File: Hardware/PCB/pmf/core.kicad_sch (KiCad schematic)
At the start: 43 parts, among them U1 AS3320, U2 TL072

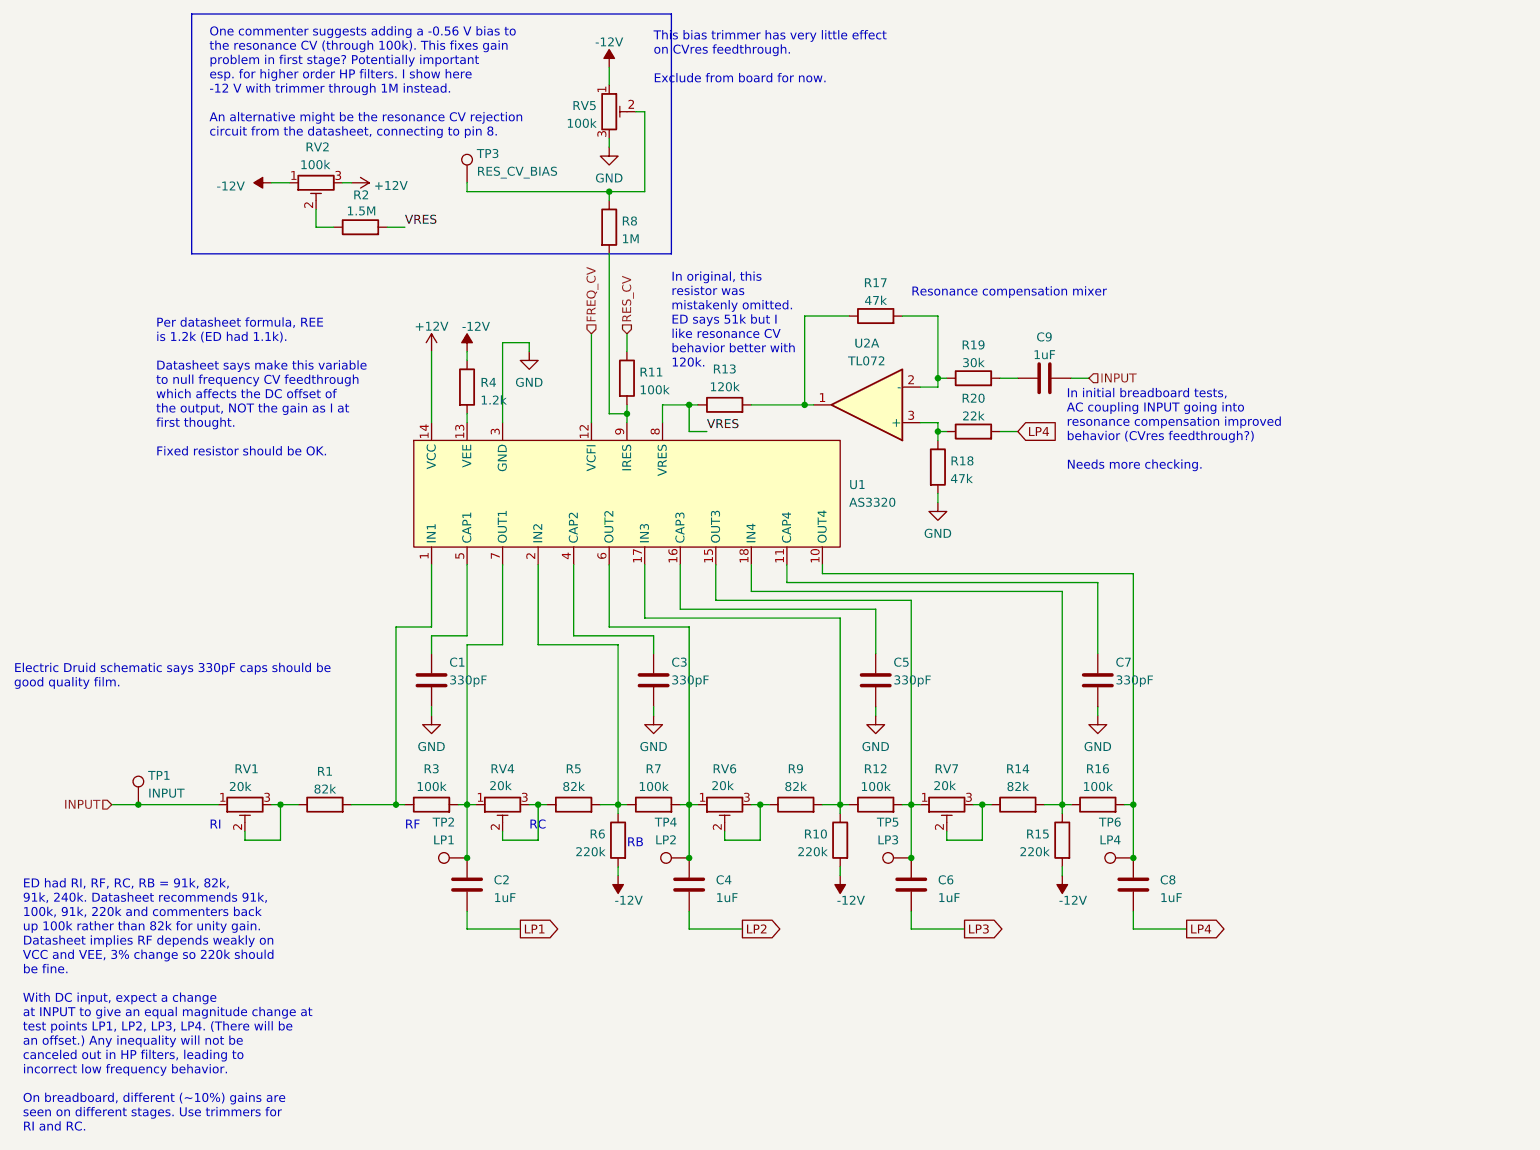
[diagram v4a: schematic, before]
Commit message: Remove VRES bias
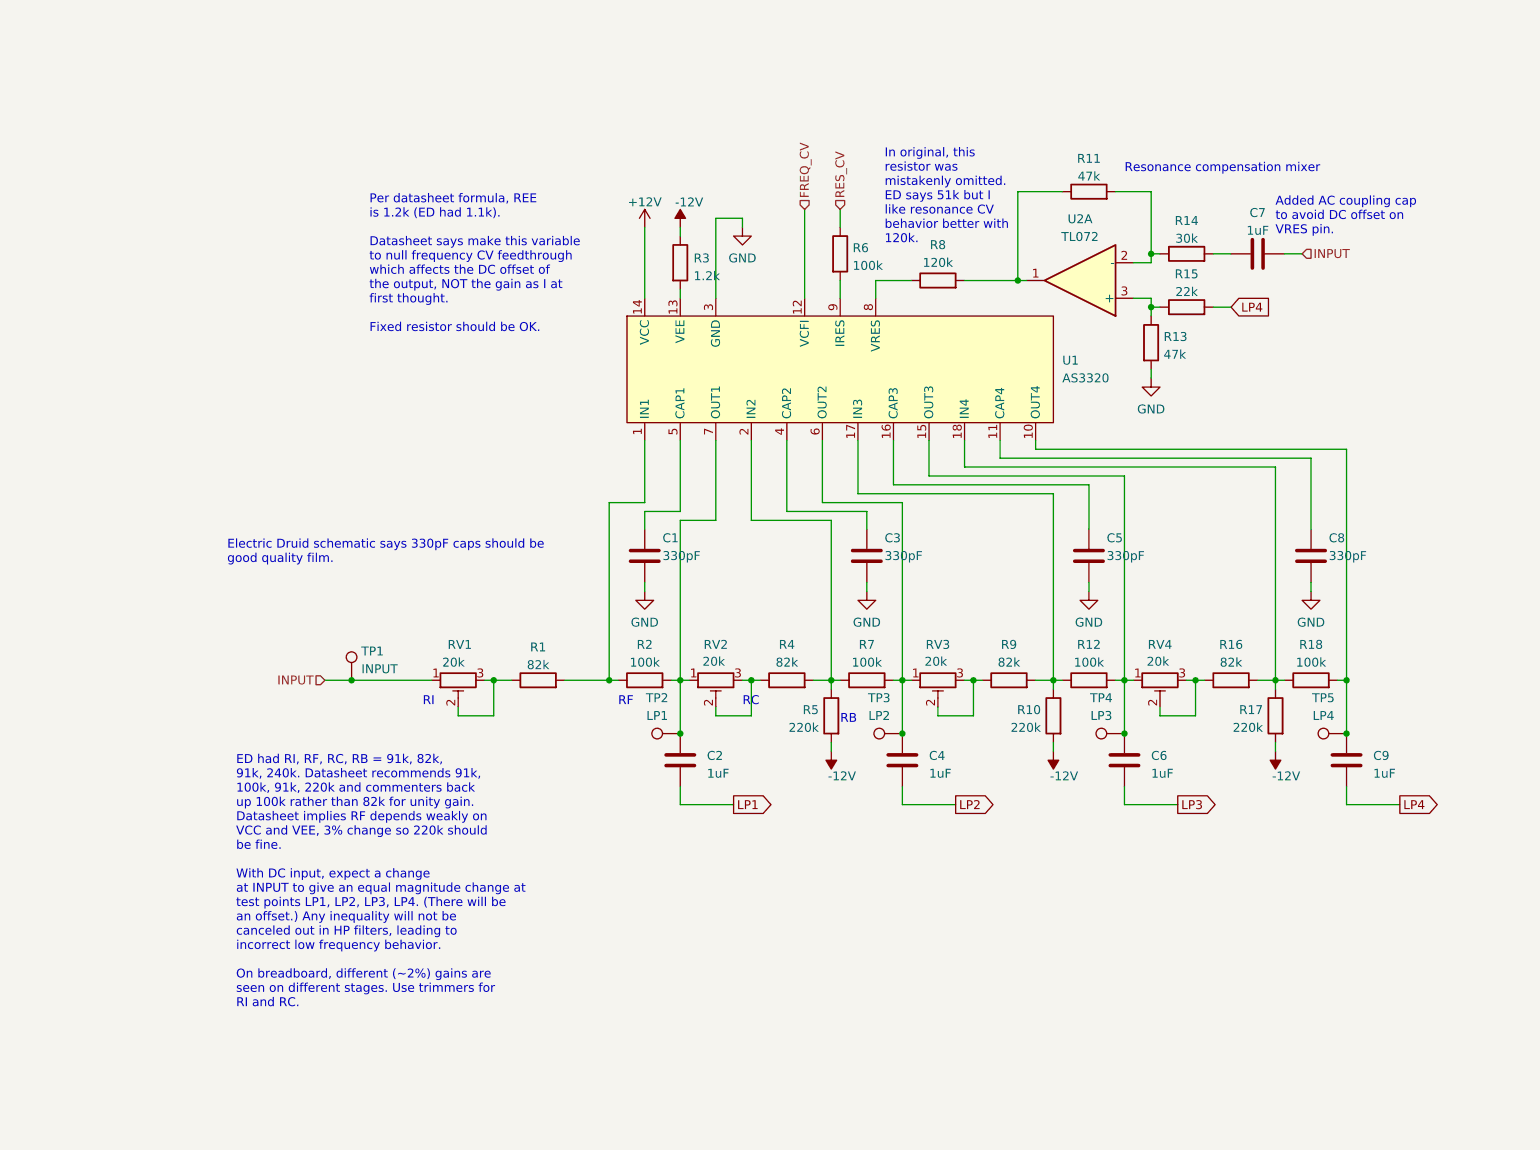
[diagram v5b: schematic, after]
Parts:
- removed R2: 1.5M, AO_tht:R_Axial_DIN0207_L6.3mm_D2.5mm_P10.16mm_Horizontal, symbol AO_symbols:R
- removed R8: 1M, AO_tht:R_Axial_DIN0207_L6.3mm_D2.5mm_P10.16mm_Horizontal, symbol AO_symbols:R
- removed RV2, RV5: 100k, AO_tht:Potentiometer_Bourns_3296W_Vertical_standard, symbol AO_symbols:R_POT_TRIM_3296W
- removed TP3: RES_CV_BIAS, AO_tht:TestPoint_THTPad_D1.5mm_Drill0.7mm, symbol AO_symbols:TestPoint
- renumbered C9 to C7, C7 to C8, C8 to C9, R17 to R11, R18 to R13, R19 to R14, R20 to R15, R14 to R16, R15 to R17, R16 to R18, R3 to R2, R4 to R3, R5 to R4, R6 to R5, R11 to R6, R13 to R8, RV4 to RV2, RV6 to RV3, RV7 to RV4, TP4 to TP3, TP5 to TP4, TP6 to TP5
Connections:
- net VRES: no longer names the net of R8.1, U1.8 (VRES)
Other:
- note added: "Added AC coupling cap to avoid DC offset on VRES pin."
- note removed: "In initial breadboard tests, AC coupling INPUT going into resonance compensation improved behavior (CVres feedthrough?) Needs more checking."
- note removed: "One commenter suggests adding a -0.56 V bias to the resonance CV (through 100k). This fixes gain problem in first stage? Potentially important esp. for higher order HP filters. I show here -12 V with trimmer through 1M instead. An alternative might be the resonance CV rejection circuit from the datasheet, connecting to pin 8."
- note removed: "This bias trimmer has very little effect on CVres feedthrough. Exclude from board for now."
- moved on the sheet: C1, C2, C3, C4, C5, C6, C7, C8, C9, R1, R10, R11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

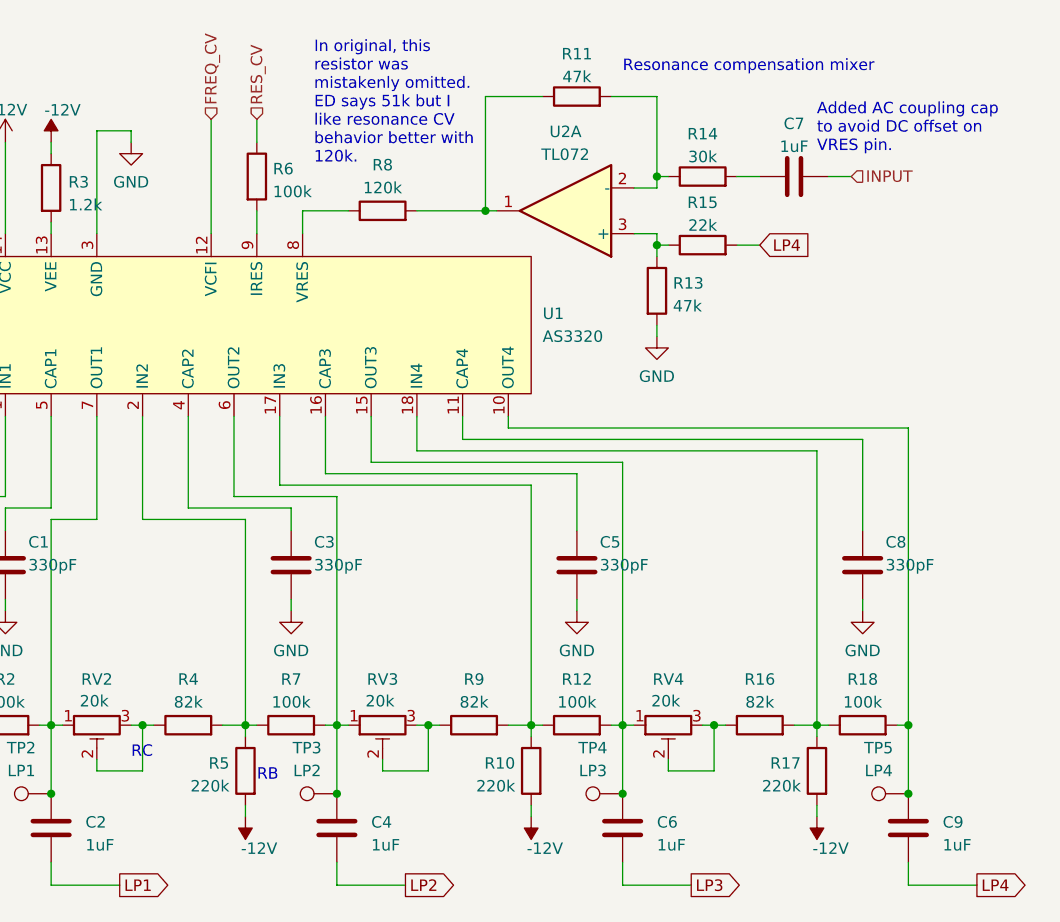
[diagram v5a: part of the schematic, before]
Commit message: CVf test point; disambiguate heirarchical symbols
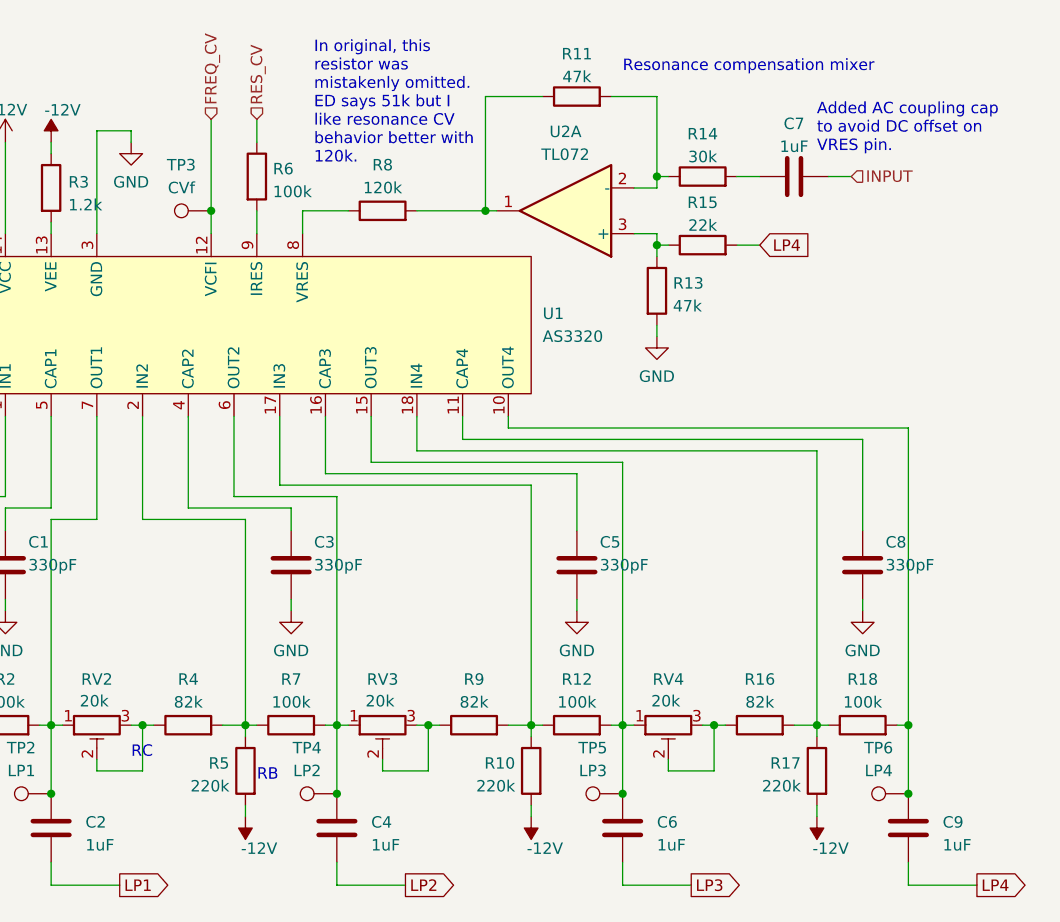
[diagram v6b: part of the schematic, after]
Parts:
- added TP3: CVf, AO_tht:TestPoint_THTPad_D1.5mm_Drill0.7mm, symbol AO_symbols:TestPoint
- renumbered TP3 to TP4, TP4 to TP5, TP5 to TP6
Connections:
- net FREQ_CV: now also TP3.1
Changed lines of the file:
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@@
   (junction (at 182.88 125.73) (diameter 0) (color 0 0 0 0)
   )
+  (junction (at 137.16 60.96) (diameter 0) (color 0 0 0 0)
+  )
   (junction (at 193.04 118.11) (diameter 0) (color 0 0 0 0)
   )
@@
     (stroke (width 0) (type default))
   )
-  (wire (pts (xy 137.16 50.8) (xy 137.16 63.5))
+  (wire (pts (xy 137.16 50.8) (xy 137.16 60.96))
     (stroke (width 0) (type default))
   )
@@
   )
   (wire (pts (xy 118.11 118.11) (xy 119.38 118.11))
+    (stroke (width 0) (type default))
+  )
+  (wire (pts (xy 137.16 60.96) (xy 137.16 63.5))
     (stroke (width 0) (type default))
   )
@@
     )
   )
+  (symbol (lib_id "AO_symbols:TestPoint") (at 137.16 60.96 90) (unit 1)
+    (in_bom no) (on_board yes) (dnp no) (fields_autoplaced)
+    (property "Reference" "TP3" (at 133.858 55.88 90)
+      (effects (font (size 1.27 1.27)))
+    )
+    (property "Value" "CVf" (at 133.858 58.42 90)
+      (effects (font (size 1.27 1.27)))
+    )
+    (property "Footprint" "AO_tht:TestPoint_THTPad_D1.5mm_Drill0.7mm" (at 137.16 55.88 0)
+      (effects (font (size 1.27 1.27)) hide)
+    )
+    (property "Datasheet" "~" (at 137.16 55.88 0)
+      (effects (font (size 1.27 1.27)) hide)
+    )
+    (property "Config" "DNF" (at 137.16 60.96 0)
+      (effects (font (size 1.27 1.27)) hide)
+    )
+    (pin "1")
+    (instances
+      (project "pmf"
+        (path "/1fce46f5-2003-4c7e-915f-b9b7dfc679d7/2085c2ec-887c-4fdb-9d07-ac0ffcad932c"
+          (reference "TP3") (unit 1)
+        )
+      )
+    )
+  )
   (symbol (lib_id "AO_symbols:R_POT_TRIM_3296W") (at 124.46 118.11 90) (mirror x) (unit 1)
     (in_bom yes) (on_board yes) (dnp no)
@@
   (symbol (lib_id "AO_symbols:TestPoint") (at 182.88 125.73 90) (unit 1)
     (in_bom no) (on_board yes) (dnp no) (fields_autoplaced)
-    (property "Reference" "TP4" (at 179.578 120.65 90)
+    (property "Reference" "TP5" (at 179.578 120.65 90)
       (effects (font (size 1.27 1.27)))
     )
@@
       (project "pmf"
         (path "/1fce46f5-2003-4c7e-915f-b9b7dfc679d7/2085c2ec-887c-4fdb-9d07-ac0ffcad932c"
-          (reference "TP4") (unit 1)
+          (reference "TP5") (unit 1)
         )
       )
@@
   (symbol (lib_id "AO_symbols:TestPoint") (at 214.63 125.73 90) (unit 1)
     (in_bom no) (on_board yes) (dnp no) (fields_autoplaced)
-    (property "Reference" "TP5" (at 211.328 120.65 90)
+    (property "Reference" "TP6" (at 211.328 120.65 90)
       (effects (font (size 1.27 1.27)))
     )
@@
       (project "pmf"
         (path "/1fce46f5-2003-4c7e-915f-b9b7dfc679d7/2085c2ec-887c-4fdb-9d07-ac0ffcad932c"
-          (reference "TP5") (unit 1)
+          (reference "TP6") (unit 1)
         )
       )
@@
   (symbol (lib_id "AO_symbols:TestPoint") (at 151.13 125.73 90) (unit 1)
     (in_bom no) (on_board yes) (dnp no) (fields_autoplaced)
-    (property "Reference" "TP3" (at 147.828 120.65 90)
+    (property "Reference" "TP4" (at 147.828 120.65 90)
       (effects (font (size 1.27 1.27)))
     )
@@
       (project "pmf"
         (path "/1fce46f5-2003-4c7e-915f-b9b7dfc679d7/2085c2ec-887c-4fdb-9d07-ac0ffcad932c"
-          (reference "TP3") (unit 1)
-        )
-      )
+          (reference "TP4") (unit 1)
+        )
+      )
